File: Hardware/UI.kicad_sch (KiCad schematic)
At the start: 0 parts

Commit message: Checkpoint
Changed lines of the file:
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@@
 (kicad_sch (version 20230121) (generator eeschema)
   (paper "A4")
+  (hierarchical_label "LED_TX" (shape input) (at 127 63.5 0) (fields_autoplaced)
+    (effects (font (size 1.27 1.27)) (justify left))
+  )
+  (hierarchical_label "SW_USER" (shape output) (at 127 60.96 0) (fields_autoplaced)
+    (effects (font (size 1.27 1.27)) (justify left))
+  )
   (hierarchical_label "VDD_3V3" (shape passive) (at 127 83.82 0) (fields_autoplaced)
     (effects (font (size 1.27 1.27)) (justify left))
   )
-  (hierarchical_label "BUZZER" (shape input) (at 127 76.2 0) (fields_autoplaced)
+  (hierarchical_label "LED_STATUS" (shape input) (at 127 68.58 0) (fields_autoplaced)
     (effects (font (size 1.27 1.27)) (justify left))
   )
-  (hierarchical_label "VDD_5V" (shape passive) (at 127 81.28 0) (fields_autoplaced)
+  (hierarchical_label "~{BUZZER}" (shape input) (at 127 76.2 0) (fields_autoplaced)
     (effects (font (size 1.27 1.27)) (justify left))
   )
+  (hierarchical_label "LED_GPS" (shape input) (at 127 71.12 0) (fields_autoplaced)
+    (effects (font (size 1.27 1.27)) (justify left))
+  )
+  (hierarchical_label "LED_RX" (shape input) (at 127 66.04 0) (fields_autoplaced)
+    (effects (font (size 1.27 1.27)) (justify left))
+  )

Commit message: Checkpoint
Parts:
- added BZ1301: Buzzer, symbol Device:Buzzer
- added D? (x4): ~, LED_SMD:LED_1206_3216Metric, symbol Device:LED_Small
- added Q?: RE1C002UN, Package_TO_SOT_SMD:SOT-416, symbol Device:Q_NMOS_GSD
- added R? (x4): 1K, Resistor_SMD:R_0805_2012Metric, symbol Device:R_Small
- added R?: 100, Resistor_SMD:R_0805_2012Metric, symbol Device:R_Small
- added R?: 2.2K, Resistor_SMD:R_0805_2012Metric, symbol Device:R_Small
- added SW?: SW_USER, Button_Switch_THT:SW_PUSH_6mm_H5mm, symbol Switch:SW_Push
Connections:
- net LED_GPS: now also R?.1
- net LED_RX: now also R?.1
- net LED_STATUS: now also R?.1
- net LED_TX: now also R?.1
- net SW_USER: now also R?.2
- net VDD_3V3: now also BZ1301.1 (-)
- net ~{BUZZER}: now also R?.1
- new net: D?.2 (A), R?.2 (x4)
- new net: BZ1301.2 (+), Q?.3 (D)
- new net: Q?.1 (G), R?.2
- new net: R?.1, SW?.2
- new net GND: D?.1 (K), D?.1 (K), D?.1 (K), D?.1 (K), Q?.2 (S), SW?.1

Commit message: Checkpoint
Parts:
- R?: value 100 -> 100R
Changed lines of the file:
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@@
       (effects (font (size 1.27 1.27)) (justify left))
     )
-    (property "Value" "100" (at 119.38 59.69 0)
+    (property "Value" "100R" (at 119.38 59.69 0)
       (effects (font (size 1.27 1.27)) (justify left))
     )

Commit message: Finalize schematic and some more routing
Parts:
- BZ1301: footprint (none) -> Buzzer_Beeper:Buzzer_12x9.5RM7.6
- R?: value 100R -> 150R; footprint Resistor_SMD:R_0805_2012Metric -> Resistor_SMD:R_0603_1608Metric
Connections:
- net VDD_3V3 renamed VDD_5V
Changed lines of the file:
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@@
-    (effects (font (size 1.27 1.27)) (justify left))
-  )
-  (hierarchical_label "VDD_3V3" (shape passive) (at 129.54 60.96 0) (fields_autoplaced)
     (effects (font (size 1.27 1.27)) (justify left))
   )
   (hierarchical_label "LED_STATUS" (shape input) (at 154.94 109.22 0) (fields_autoplaced)
+    (effects (font (size 1.27 1.27)) (justify left))
+  )
+  (hierarchical_label "VDD_5V" (shape passive) (at 129.54 60.96 0) (fields_autoplaced)
     (effects (font (size 1.27 1.27)) (justify left))
   )
@@
       (effects (font (size 1.27 1.27)) (justify left))
     )
-    (property "Footprint" "" (at 131.445 66.04 90)
+    (property "Footprint" "Buzzer_Beeper:Buzzer_12x9.5RM7.6" (at 131.445 66.04 90)
       (effects (font (size 1.27 1.27)) hide)
     )
@@
       (effects (font (size 1.27 1.27)) (justify left))
     )
-    (property "Value" "100R" (at 119.38 59.69 0)
+    (property "Value" "150R" (at 119.38 59.69 0)
       (effects (font (size 1.27 1.27)) (justify left))
     )
-    (property "Footprint" "Resistor_SMD:R_0805_2012Metric" (at 116.84 58.42 0)
+    (property "Footprint" "Resistor_SMD:R_0603_1608Metric" (at 116.84 58.42 0)
       (effects (font (size 1.27 1.27)) hide)
     )

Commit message: Finalize silkscreen
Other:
- title: (none) -> Avionus_Flight_Controller
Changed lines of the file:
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@@
 (kicad_sch (version 20230121) (generator eeschema)
   (paper "A4")
+  (title_block
+    (title "Avionus_Flight_Controller")
+    (date "2023-11-25")
+    (rev "1.0")
+  )
   (junction (at 139.7 109.22) (diameter 0) (color 0 0 0 0)
   )

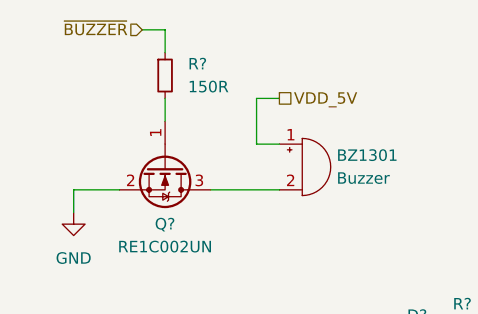
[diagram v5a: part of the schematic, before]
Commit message: Fix buzzer polarity and UI power domain notation
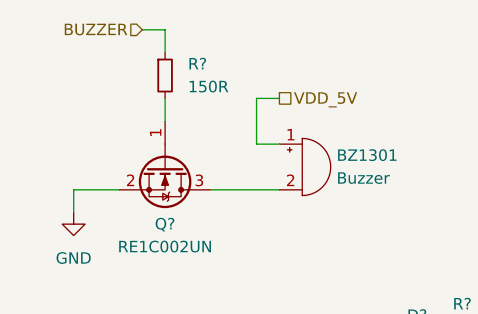
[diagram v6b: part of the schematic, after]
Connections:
- net ~{BUZZER} renamed BUZZER
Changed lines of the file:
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@@
     (effects (font (size 1.27 1.27)) (justify left))
   )
-  (hierarchical_label "~{BUZZER}" (shape input) (at 114.3 53.34 180) (fields_autoplaced)
+  (hierarchical_label "BUZZER" (shape input) (at 114.3 53.34 180) (fields_autoplaced)
     (effects (font (size 1.27 1.27)) (justify right))
   )
